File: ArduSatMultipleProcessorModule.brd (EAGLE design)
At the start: 95.5 x 90.3 mm, 268 parts, among them IC1 ATMEGA328P, IC10 ATMEGA328P, IC11 ATMEGA328P, IC12 ATMEGA328P, IC13 ATMEGA328P, IC14 ATMEGA328P, IC15 ATMEGA328P, IC16 ATMEGA328P, IC17 ATMEGA328P, IC18 ATMEGA328P, IC2 ATMEGA328P, IC3 ATMEGA328P, IC4 ATMEGA328P, IC5 ATMEGA328P, IC6 ATMEGA328P, IC7 ATMEGA328P, IC8 MCP23S17ML, IC9 ATMEGA328P, P1 N1_ICSP, P10 N0_ICSP, P11 N1_ICSP, P12 N0_ICSP, P13 N1_ICSP, P14 N0_ICSP, P15 N1_ICSP, P16 N0_ICSP, P17 N1_ICSP, P2 N0_ICSP, P3 N0_ICSP, P4 N1_ICSP, P5 N1_ICSP, P6 N0_ICSP, P7 N1_ICSP, P8 N0_ICSP, P9 N1_ICSP, Q1 BSS138 N-MOSFET, Q10 2N7002 N-MOSFET, Q11 BSS138 N-MOSFET, Q12 BSS138 N-MOSFET, Q13 2N7002 N-MOSFET, Q14 2N7002 N-MOSFET, Q15 BSS138 N-MOSFET, Q16 BSS138 N-MOSFET, Q17 BSS138 N-MOSFET, Q18 BSS138 N-MOSFET, Q19 BSS138 N-MOSFET, Q2 BSS138 N-MOSFET, Q20 BSS138 N-MOSFET, Q21 BSS138 N-MOSFET, Q22 BSS138 N-MOSFET, Q23 2N7002 N-MOSFET, Q24 2N7002 N-MOSFET, Q25 2N7002 N-MOSFET, Q26 2N7002 N-MOSFET, Q27 BSS138 N-MOSFET, Q28 BSS138 N-MOSFET, Q29 BSS138 N-MOSFET, Q3 BSS138 N-MOSFET, Q30 BSS138 N-MOSFET, Q31 BSS138 N-MOSFET, Q32 BSS138 N-MOSFET, Q33 BSS138 N-MOSFET, Q34 BSS138 N-MOSFET, Q35 2N7002 N-MOSFET, Q36 2N7002 N-MOSFET, Q37 2N7002 N-MOSFET, Q38 2N7002 N-MOSFET, Q39 BSS138 N-MOSFET, Q4 BSS138 N-MOSFET, Q40 BSS138 N-MOSFET, Q41 BSS138 N-MOSFET, Q42 BSS138 N-MOSFET, Q43 BSS138 N-MOSFET, Q44 BSS138 N-MOSFET, Q45 BSS138 N-MOSFET, Q46 BSS138 N-MOSFET, Q47 2N7002 N-MOSFET, Q48 2N7002 N-MOSFET, Q49 2N7002 N-MOSFET, Q5 BSS138 N-MOSFET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

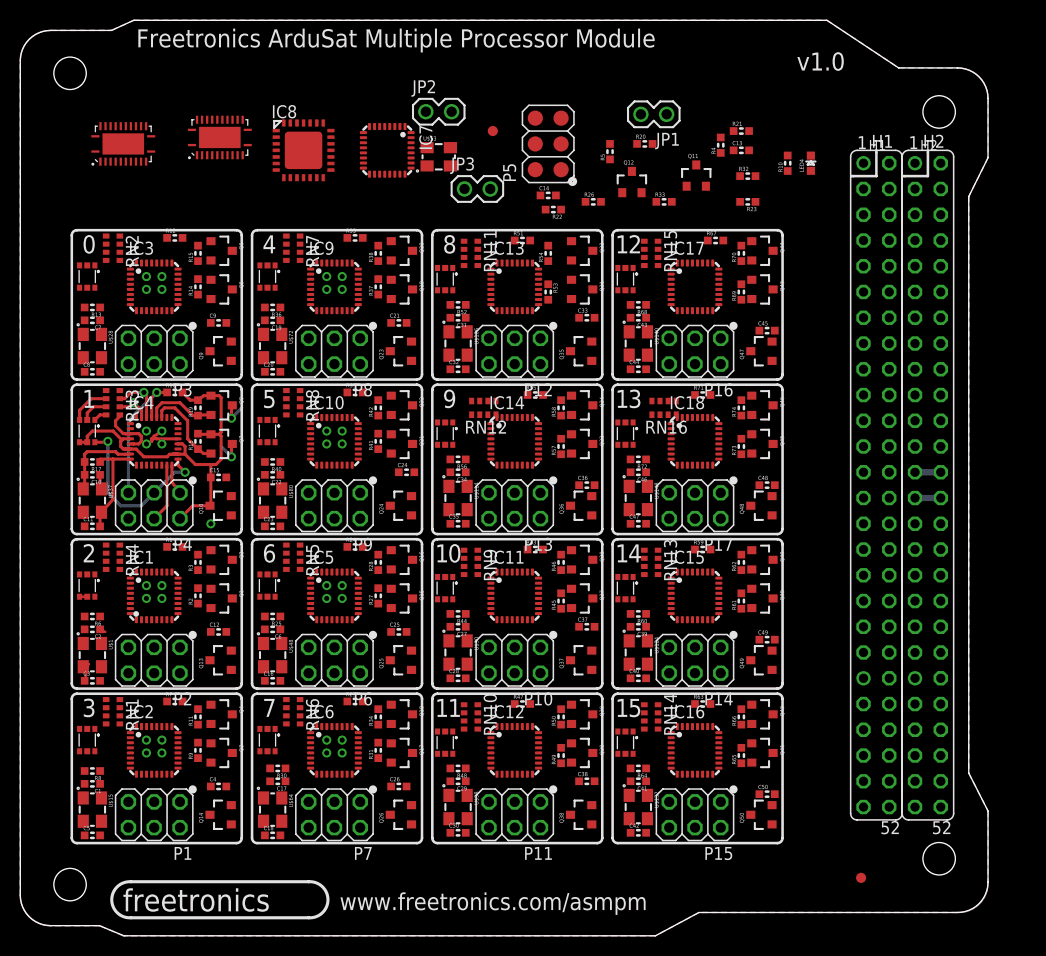
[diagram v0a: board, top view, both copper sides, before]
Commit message: Routing processor nodes
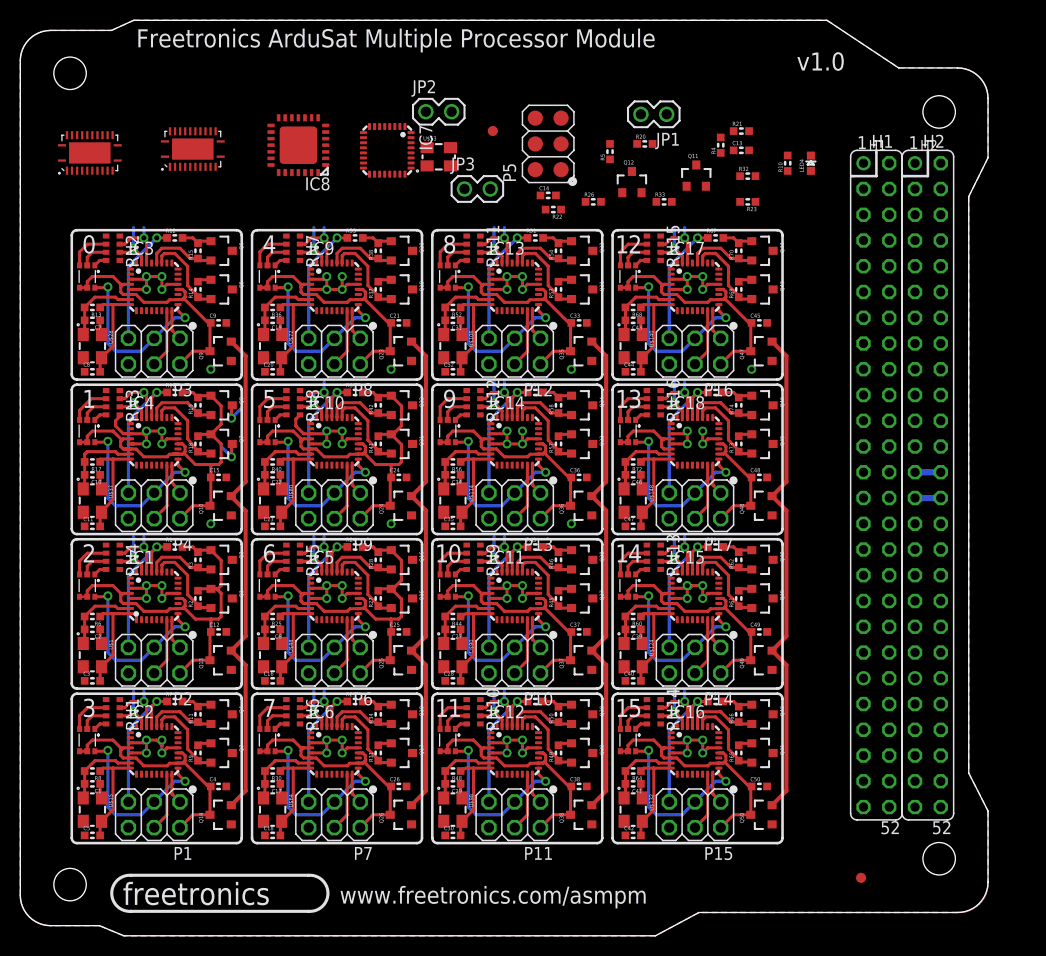
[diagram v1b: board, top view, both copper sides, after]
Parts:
- moved U$59 3.42 mm to (6.86, 77.2)
- moved U$60 2.90 mm to (17.0, 77.6)
- moved R51 1.30 mm to (50.8, 68.8)
- moved R47 1.30 mm to (50.8, 23.1)
- moved R63 1.30 mm to (68.6, 23.1)
- moved R59 1.30 mm to (68.6, 38.4)
- moved R71 1.30 mm to (68.6, 53.6)
- moved RN12 1.14 mm to (44.7, 52.6), turned to 90 degrees
- moved RN16 1.14 mm to (62.5, 52.6), turned to 90 degrees
- moved C36 1.08 mm to (55.1, 45.2)
- moved C45 1.08 mm to (72.9, 60.5)
- moved C48 1.08 mm to (72.9, 45.2)
- moved C49 1.08 mm to (72.9, 30.0)
- moved C50 1.08 mm to (72.9, 14.7)
- moved R53 1.05 mm to (53.1, 63.8), turned to 90 degrees
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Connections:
- net N14_D13_SCK: now also U$125.4
- net N6_D13_SCK: no longer U$125.4
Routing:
- net +5V_SYS: track 2.54 -> 199.5 mm
- net GND: track 15.5 -> 176.0 mm, vias 33 -> 71
- net N6_5V: track 0.00 -> 39.7 mm
- net N5_5V: track 0.00 -> 39.7 mm
- net N2_5V: track 0.75 -> 39.4 mm
- net N9_5V: track 0.00 -> 29.7 mm
- net N15_5V: track 0.00 -> 29.7 mm
- net N4_5V: track 0.00 -> 29.7 mm
- net N12_5V: track 0.00 -> 29.7 mm
- net N3_5V: track 0.00 -> 29.7 mm
- net N11_5V: track 0.00 -> 29.7 mm
- net N14_5V: track 0.00 -> 29.7 mm
- net N10_5V: track 0.00 -> 29.7 mm
- net N7_5V: track 0.00 -> 29.7 mm
- net N0_5V: track 0.00 -> 29.7 mm
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
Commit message: Routing
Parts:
- moved U$59 77.3 mm to (79.9, 51.8)
- moved U$60 73.2 mm to (79.9, 40.1)
- moved IC8 56.0 mm to (80.1, 58.9)
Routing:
- net NODE_SDA: track 2.74 -> 110.2 mm, vias 1 -> 8
- net NODE_SCL: track 2.74 -> 110.2 mm, vias 1 -> 8
- net N11_5V: track 29.7 -> 39.7 mm
- net N15_5V: track 29.7 -> 39.7 mm
- net N4_5V: track 29.7 -> 39.7 mm
- net N10_5V: track 29.7 -> 39.7 mm
- net N13_5V: track 24.6 -> 34.6 mm
- net N12_5V: track 29.7 -> 39.7 mm
- net N7_5V: track 29.7 -> 39.7 mm
- net N14_5V: track 29.7 -> 39.7 mm
- net N3_5V: track 29.7 -> 39.7 mm
- net N8_5V: track 29.6 -> 39.5 mm
- net N0_5V: track 29.7 -> 39.6 mm
- net N9_5V: track 29.7 -> 38.5 mm
- net GND: vias 71 -> 80

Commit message: Routing
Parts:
- P5: device freetronics-jon:2X03SURFACE -> freetronics-jon:2X03PTH
- moved IC8 69.6 mm to (12.7, 76.2)
- moved U$60 58.7 mm to (33.5, 76.1), turned to 90 degrees
- moved U$59 46.3 mm to (41.1, 77.2)
- moved P5 27.9 mm to (80.0, 78.1)
- moved IC7 15.2 mm to (51.4, 77.5), turned to 180 degrees
- moved U$53 14.3 mm to (55.2, 80.0)
- moved JP1 2.54 mm to (66.3, 81.0)
- moved C39 1.91 mm to (62.4, 30.2)
- moved C40 1.91 mm to (62.4, 25.1)
- moved C41 1.91 mm to (62.4, 15.0)
- moved C42 1.91 mm to (62.4, 9.91)
- moved C43 1.91 mm to (62.4, 60.7)
- moved C44 1.91 mm to (62.4, 55.6)
- moved C45 1.91 mm to (74.8, 60.5)
- moved C46 1.91 mm to (62.4, 45.5)
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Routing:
- net NODE_SCL: track 110.2 -> 337.8 mm, vias 8 -> 16
- net NODE_SDA: track 110.2 -> 313.8 mm, vias 8 -> 16
- net +5V_SYS: track 199.5 -> 276.2 mm
- net N3_PWR: track 0.00 -> 70.9 mm, vias 0 -> 2
- net N7_PWR: track 0.00 -> 63.9 mm, vias 0 -> 1
- net N15_PWR: track 0.00 -> 63.9 mm, vias 0 -> 1
- net N2_PWR: track 0.00 -> 55.6 mm, vias 0 -> 2
- net N11_PWR: track 0.00 -> 53.1 mm, vias 0 -> 1
- net N7_D0_RX: track 6.23 -> 59.1 mm
- net N3_D0_RX: track 6.23 -> 59.1 mm
- net N15_D0_RX: track 6.23 -> 59.1 mm
- net N11_D0_RX: track 6.23 -> 59.1 mm
- net N3_D1_TX: track 5.34 -> 57.7 mm
- net N15_D1_TX: track 5.34 -> 57.6 mm
- net N7_D1_TX: track 5.34 -> 57.6 mm
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
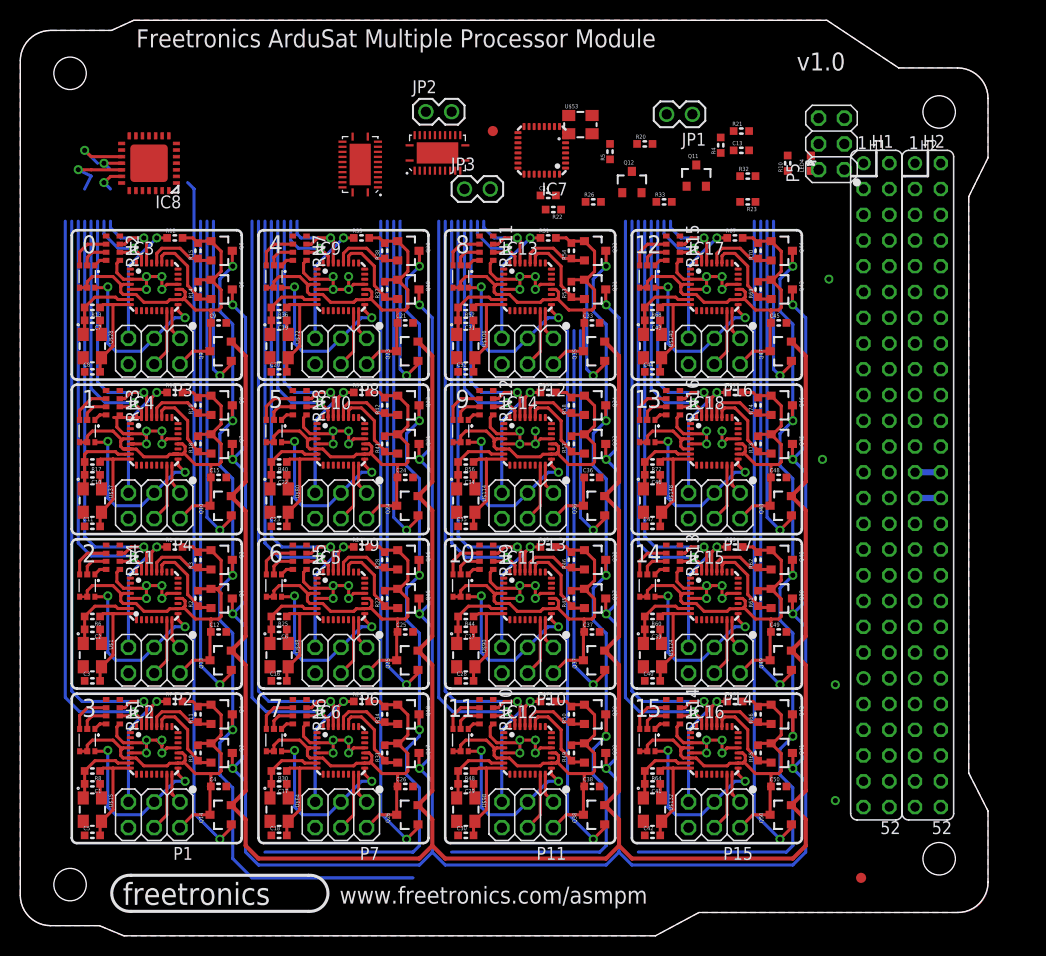
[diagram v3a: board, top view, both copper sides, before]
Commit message: Experiments with arrangements of UART and PWR control
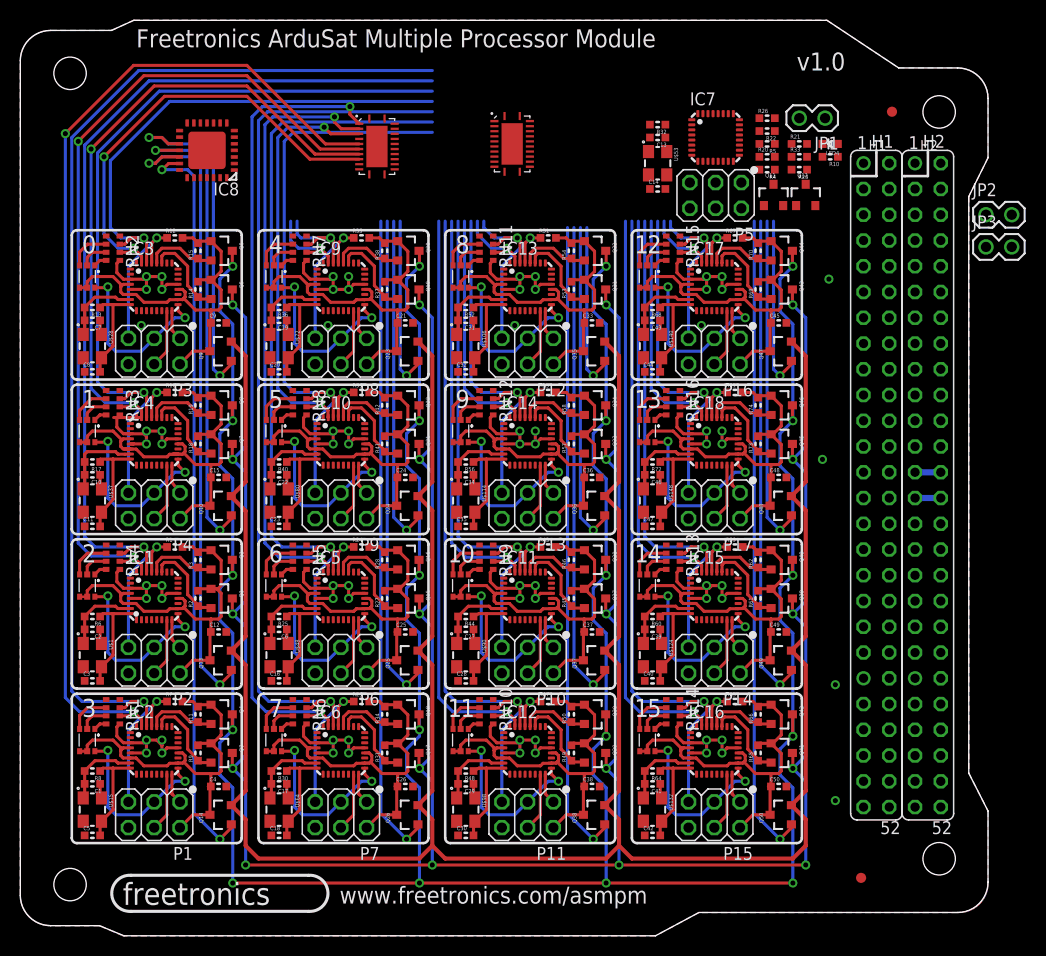
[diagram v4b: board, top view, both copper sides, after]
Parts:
- moved JP2 56.2 mm to (95.2, 71.1)
- moved JP3 51.8 mm to (95.2, 67.9)
- moved U$21 39.4 mm to (86.0, 81.3)
- moved R22 22.5 mm to (73.7, 79.4)
- moved R26 19.0 mm to (73.7, 80.6)
- moved IC7 17.2 mm to (68.6, 78.7), turned to 0 degrees
- moved Q12 17.2 mm to (77.5, 73.0)
- moved R5 15.5 mm to (73.7, 78.1), turned to 180 degrees
- moved R33 14.1 mm to (76.8, 76.8)
- moved JP1 13.1 mm to (79.4, 80.6)
- moved P5 12.5 mm to (68.6, 73.0), turned to 180 degrees
- moved R20 12.1 mm to (73.7, 76.8)
- moved C14 10.8 mm to (62.9, 73.7)
- moved R32 10.2 mm to (62.9, 80.0), turned to 180 degrees
- moved U$53 8.52 mm to (62.9, 76.2), turned to 270 degrees
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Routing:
- net N3_D0_RX: track 59.1 -> 105.7 mm
- net N2_D0_RX: track 42.6 -> 87.0 mm
- net N3_D1_TX: track 57.7 -> 101.4 mm, vias 1 -> 2
- net N1_D0_RX: track 26.1 -> 68.4 mm
- net N2_D1_TX: track 41.2 -> 82.4 mm, vias 1 -> 2
- net N0_D0_RX: track 9.57 -> 49.7 mm
- net N1_D1_TX: track 27.3 -> 66.3 mm, vias 1 -> 2
- net N0_D1_TX: track 8.08 -> 44.6 mm, vias 1 -> 2
- net N7_D0_RX: track 59.1 -> 86.5 mm
- net N6_D0_RX: track 42.6 -> 67.6 mm
- net N5_D0_RX: track 26.1 -> 48.9 mm
- net N7_D1_TX: track 57.6 -> 80.0 mm, vias 1 -> 2
- net N6_D1_TX: track 41.1 -> 61.0 mm, vias 1 -> 2
- net N5_D1_TX: track 24.6 -> 41.6 mm, vias 1 -> 2
- net N0_PWR: track 23.1 -> 34.6 mm
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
